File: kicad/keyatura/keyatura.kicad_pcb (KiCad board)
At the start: 2 copper layers, 256.5 x 126.2 mm, 93 parts, among them J1 Battery, SW1 SW_Push, SW10 SW_Push, SW11 SW_Push, SW12 SW_Push, SW13 SW_Push, SW14 SW_Push, SW15 SW_Push, SW16 SW_Push, SW17 SW_Push, SW18 SW_Push, SW19 SW_Push, SW2 SW_Push, SW20 SW_Push, SW21 SW_Push, SW22 SW_Push, SW23 SW_Push, SW24 SW_Push, SW25 SW_Push, SW26 SW_Push, SW27 SW_Push, SW28 SW_Push, SW29 SW_Push, SW3 SW_Push, SW30 SW_Push, SW31 SW_Push, SW32 SW_Push, SW33 SW_Push, SW34 SW_Push, SW35 SW_Push, SW36 SW_Push, SW4 SW_Push, SW5 SW_Push, SW6 SW_Push, SW7 SW_Push, SW8 SW_Push, SW9 SW_Push, U1 SuperMini nRF52840

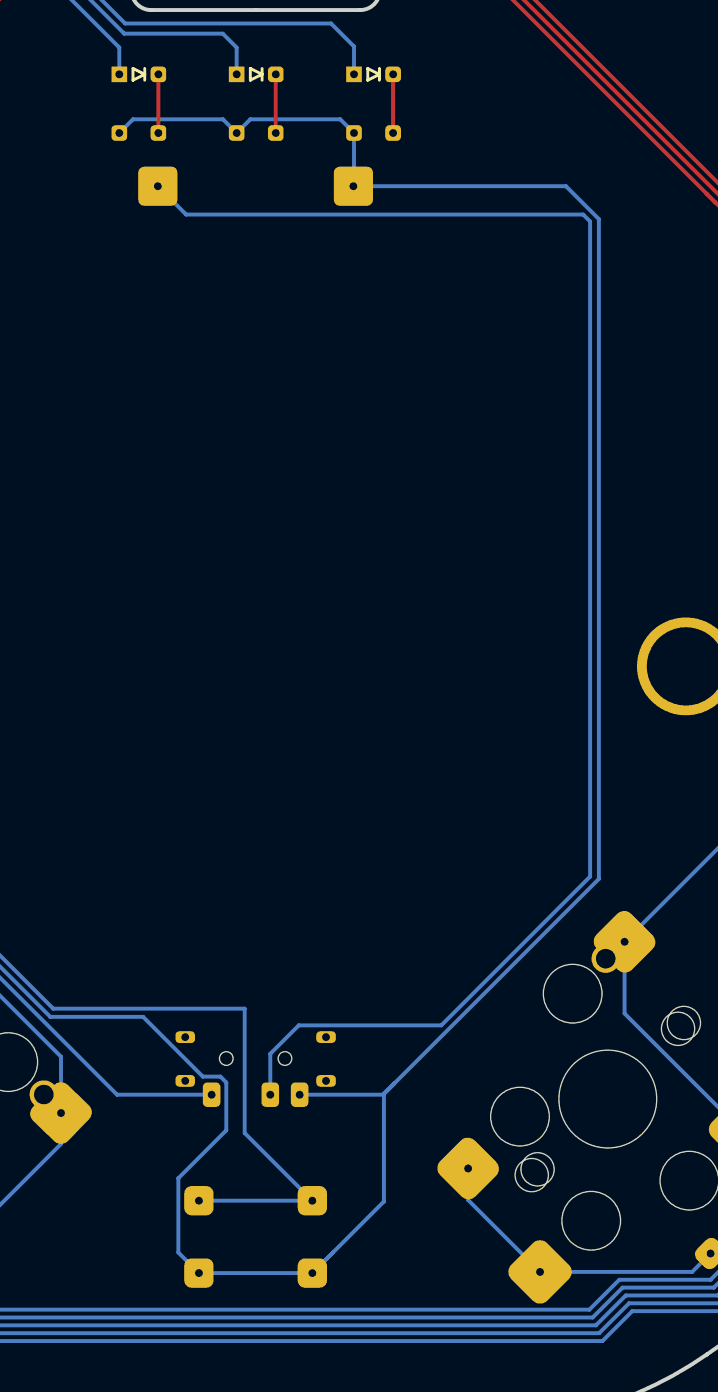
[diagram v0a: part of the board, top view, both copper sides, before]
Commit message: fixed fatal bug of connected B- and B+ while turning off battery
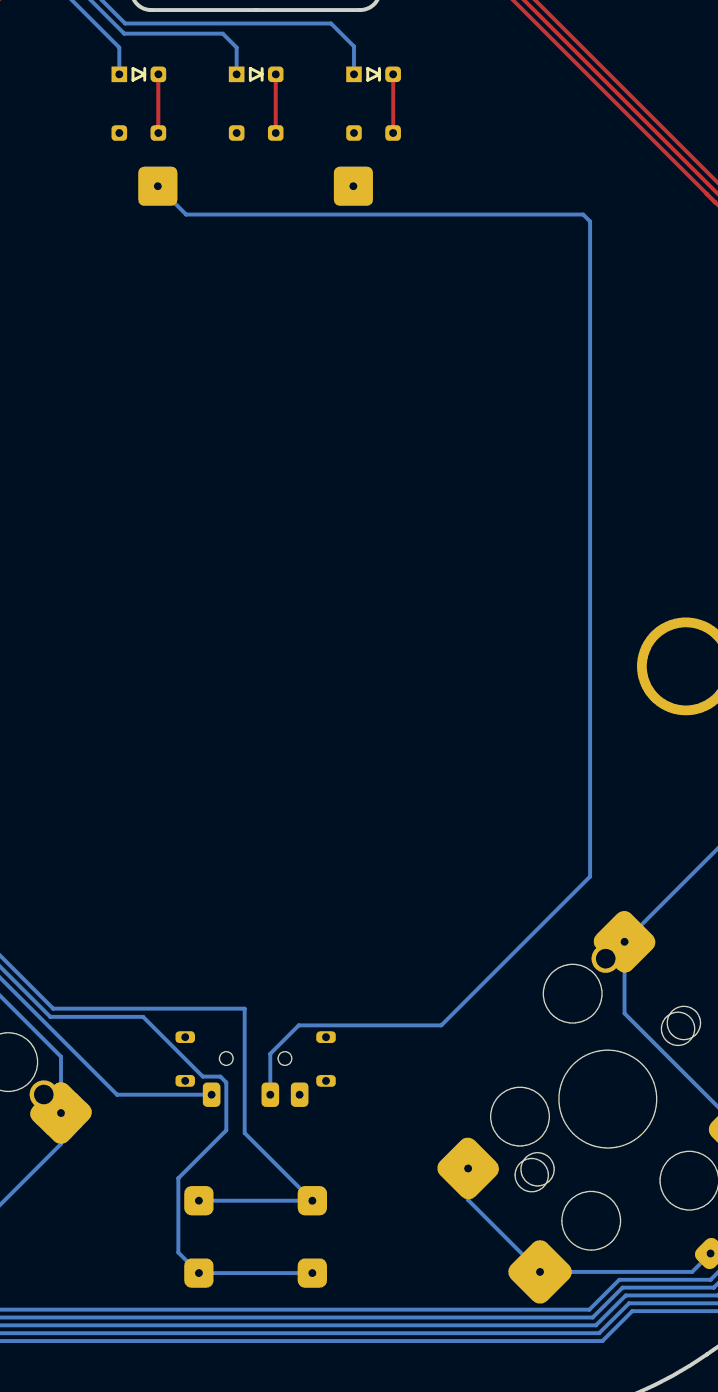
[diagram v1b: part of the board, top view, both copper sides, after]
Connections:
- BAT_KEY1 pad 3: GND -> unconnected-(BAT_KEY1-C-Pad3)
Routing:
- net GND: track 209.1 -> 113.5 mm
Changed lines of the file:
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@@
 	(net 61 "Net-(L2-K)")
 	(net 62 "RST")
+	(net 63 "unconnected-(BAT_KEY1-C-Pad3)")
 	(footprint "key-switches:SW_MX_Kailh_Choc_V1V2_HotSwap_Hybrid"
 		(layer "F.Cu")
@@
 			(remove_unused_layers no)
 			(roundrect_rratio 0.25)
-			(net 52 "GND")
+			(net 63 "unconnected-(BAT_KEY1-C-Pad3)")
 			(pinfunction "C")
 			(pintype "passive")
@@
 	)
 	(segment
-		(start 172 92.132958)
-		(end 172 125.867042)
-		(width 0.2)
-		(layer "B.Cu")
-		(net 52)
-	)
-	(segment
 		(start 152.951 138.72)
 		(end 152.951 136.27589)
@@
 	)
 	(segment
-		(start 158.779 87.029)
-		(end 159.48 87.73)
-		(width 0.2)
-		(layer "B.Cu")
-		(net 52)
-	)
-	(segment
 		(start 151.75089 135.974)
 		(end 148.69689 132.92)
@@
 	)
 	(segment
-		(start 147.48 87.73)
-		(end 148.181 87.029)
-		(width 0.2)
-		(layer "B.Cu")
-		(net 52)
-	)
-	(segment
 		(start 136.899 125.866042)
 		(end 136.899 63.851)
@@
 	)
 	(segment
-		(start 161.553521 136.313521)
-		(end 160.967042 136.9)
-		(width 0.2)
-		(layer "B.Cu")
-		(net 52)
-	)
-	(segment
 		(start 150.499 144.969)
 		(end 150.499 141.172)
@@
 	)
 	(segment
-		(start 161.01 136.857042)
-		(end 161.553521 136.313521)
-		(width 0.2)
-		(layer "B.Cu")
-		(net 52)
-	)
-	(segment
-		(start 160.967042 136.9)
-		(end 156.7 136.9)
-		(width 0.2)
-		(layer "B.Cu")
-		(net 52)
-	)
-	(segment
 		(start 152.951 136.27589)
 		(end 152.64911 135.974)
@@
 	)
 	(segment
-		(start 152.779 87.029)
-		(end 153.48 87.73)
-		(width 0.2)
-		(layer "B.Cu")
-		(net 52)
-	)
-	(segment
-		(start 148.181 87.029)
-		(end 152.779 87.029)
-		(width 0.2)
-		(layer "B.Cu")
-		(net 52)
-	)
-	(segment
-		(start 158.401 144.969)
-		(end 157.35 146.02)
-		(width 0.2)
-		(layer "B.Cu")
-		(net 52)
-	)
-	(segment
-		(start 161.01 142.36)
-		(end 161.01 136.857042)
-		(width 0.2)
-		(layer "B.Cu")
-		(net 52)
-	)
-	(segment
-		(start 159.48 90.35)
-		(end 159.48 87.73)
-		(width 0.2)
-		(layer "B.Cu")
-		(net 52)
-	)
-	(segment
 		(start 148.69689 132.92)
 		(end 143.952958 132.92)
@@
 	(segment
 		(start 159.45 90.45)
-		(end 170.317042 90.45)
-		(width 0.2)
-		(layer "B.Cu")
-		(net 52)
-	)
-	(segment
-		(start 153.48 87.73)
-		(end 154.181 87.029)
-		(width 0.2)
-		(layer "B.Cu")
-		(net 52)
-	)
-	(segment
-		(start 172 125.867042)
-		(end 161.553521 136.313521)
-		(width 0.2)
-		(layer "B.Cu")
-		(net 52)
-	)
-	(segment
-		(start 159.45 90.45)
 		(end 159.45 90.38)
 		(width 0.2)
@@
 	)
 	(segment
-		(start 170.317042 90.45)
-		(end 172 92.132958)
-		(width 0.2)
-		(layer "B.Cu")
-		(net 52)
-	)
-	(segment
 		(start 157.35 146.02)
 		(end 151.55 146.02)
@@
 		(width 0.2)
 		(layer "B.Cu")
-		(net 52)
-	)
-	(segment
-		(start 154.181 87.029)
-		(end 158.779 87.029)
-		(width 0.2)
-		(layer "B.Cu")
-		(net 52)
-	)
-	(segment
-		(start 157.35 146.02)
-		(end 161.01 142.36)
-		(width 0.2)
-		(layer "B.Cu")
